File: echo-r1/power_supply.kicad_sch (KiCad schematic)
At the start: 26 parts, among them J1 GT-BTP30003-xxxA-16A, Q2 AO3401A, U1 LM66100DCK, U2 TPS62A01DRLR, U3 TPS62A01DRLR, U4 XC6206P33xMR, U5 TP4057

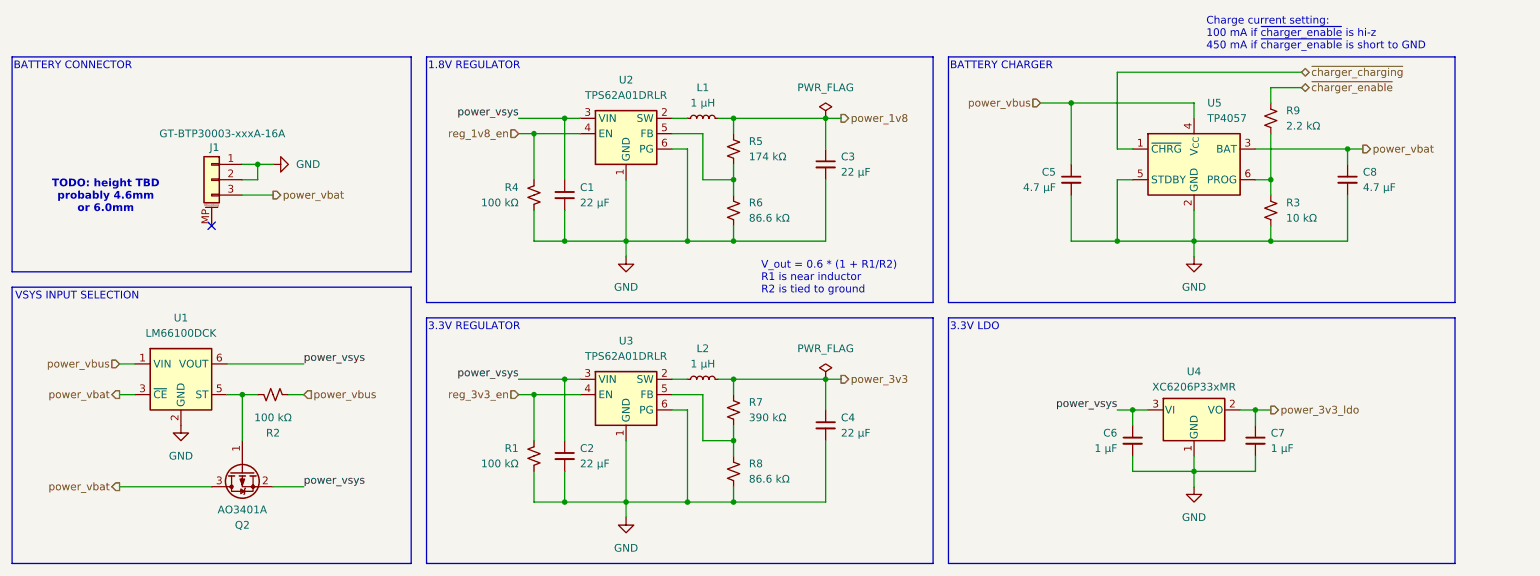
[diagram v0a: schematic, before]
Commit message: WIP redesign with STM32H7R3Z8J6
The H7R3 has a bunch of features that greatly simplify the design:
support for HyperRAM, which requires far fewer pins than SDRAM and
is more power efficient; this frees up the FMC to interface with the
display in 8-bit 8080 MCU mode; and there is a built-in USB HS PHY,
removing the need for an external PHY.

The huge reduction in signal count allows for a smaller pin count
package -- only 144 pins. HyperRAM only comes in BGA packages so it
makes sense to also use the UFBGA-144 package for the CPU, which
takes up less than 1/4 of the board area of an LQFP-176 package.
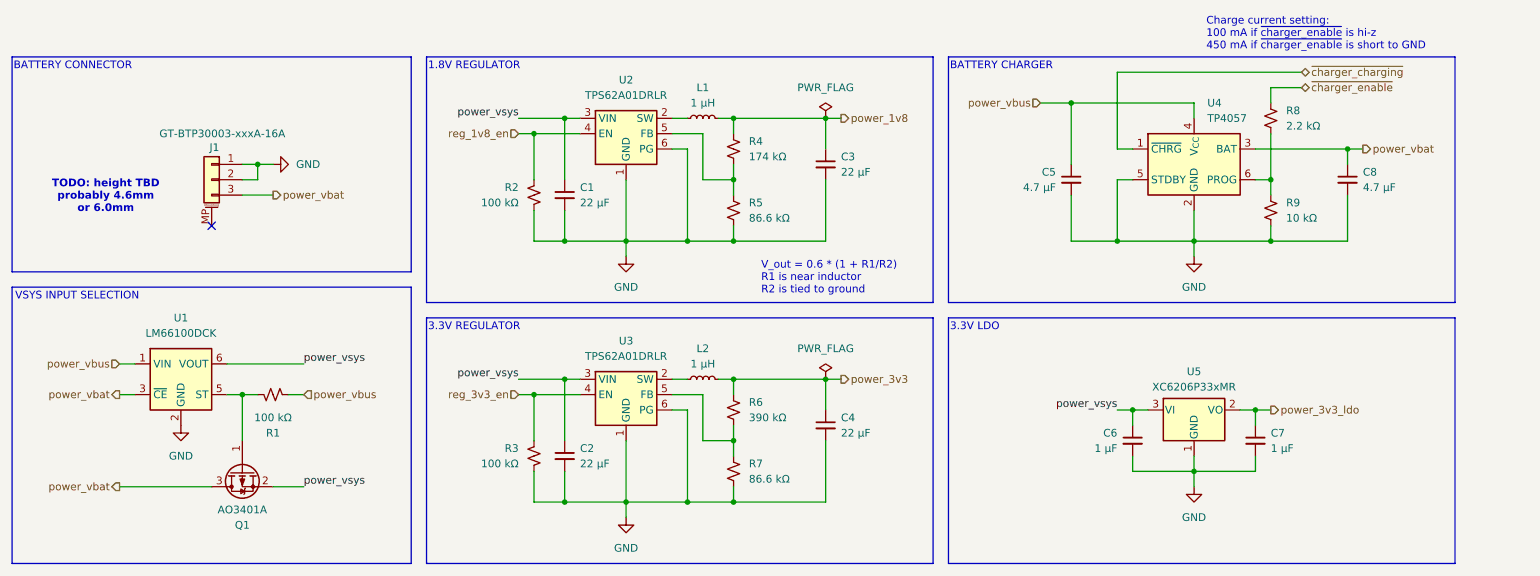
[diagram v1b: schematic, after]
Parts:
- renumbered Q2 to Q1, R2 to R1, R4 to R2, R1 to R3, R5 to R4, R6 to R5, R7 to R6, R8 to R7, R9 to R8, R3 to R9, U5 to U4, U4 to U5
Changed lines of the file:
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@@
 		(dnp no)
 		(fields_autoplaced yes)
-		(property "Reference" "#FLG02"
+		(property "Reference" "#FLG03"
 			(at 162.56 92.075 0)
 			(effects
@@
 			(project "echo-r1"
 				(path "/aa241847-30f4-429d-a148-6a6e39ba98e0/48d39f5c-11a4-46cd-927a-56a9c6ae42fa"
-					(reference "#FLG02")
+					(reference "#FLG03")
 					(unit 1)
 				)
@@
 		(on_board yes)
 		(dnp no)
-		(property "Reference" "R4"
+		(property "Reference" "R2"
 			(at 111.76 62.2299 0)
 			(effects
@@
 			(project "echo-r1"
 				(path "/aa241847-30f4-429d-a148-6a6e39ba98e0/48d39f5c-11a4-46cd-927a-56a9c6ae42fa"
-					(reference "R4")
+					(reference "R2")
 					(unit 1)
 				)
@@
 		(dnp no)
 		(fields_autoplaced yes)
-		(property "Reference" "U5"
+		(property "Reference" "U4"
 			(at 225.7141 48.26 0)
 			(effects
@@
 			(project ""
 				(path "/aa241847-30f4-429d-a148-6a6e39ba98e0/48d39f5c-11a4-46cd-927a-56a9c6ae42fa"
-					(reference "U5")
+					(reference "U4")
 					(unit 1)
 				)
@@
 		(on_board yes)
 		(dnp no)
-		(property "Reference" "R3"
+		(property "Reference" "R9"
 			(at 238.76 64.7699 0)
 			(effects
@@
 			(project "echo-r1"
 				(path "/aa241847-30f4-429d-a148-6a6e39ba98e0/48d39f5c-11a4-46cd-927a-56a9c6ae42fa"
-					(reference "R3")
+					(reference "R9")
 					(unit 1)
 				)
@@
 		(dnp no)
 		(fields_autoplaced yes)
-		(property "Reference" "R6"
+		(property "Reference" "R5"
 			(at 149.86 64.7699 0)
 			(effects
@@
 			(project "echo-r1"
 				(path "/aa241847-30f4-429d-a148-6a6e39ba98e0/48d39f5c-11a4-46cd-927a-56a9c6ae42fa"
-					(reference "R6")
+					(reference "R5")
 					(unit 1)
 				)
@@
 		(on_board yes)
 		(dnp no)
-		(property "Reference" "Q2"
+		(property "Reference" "Q1"
 			(at 66.04 118.11 90)
 			(effects
@@
 			(project "echo-r1"
 				(path "/aa241847-30f4-429d-a148-6a6e39ba98e0/48d39f5c-11a4-46cd-927a-56a9c6ae42fa"
-					(reference "Q2")
+					(reference "Q1")
 					(unit 1)
 				)
@@
 		(dnp no)
 		(fields_autoplaced yes)
-		(property "Reference" "#PWR016"
+		(property "Reference" "#PWR014"
 			(at 223.52 80.01 0)
 			(effects
@@
 			(project ""
 				(path "/aa241847-30f4-429d-a148-6a6e39ba98e0/48d39f5c-11a4-46cd-927a-56a9c6ae42fa"
-					(reference "#PWR016")
+					(reference "#PWR014")
 					(unit 1)
 				)
@@
 		(on_board yes)
 		(dnp no)
-		(property "Reference" "R1"
+		(property "Reference" "R3"
 			(at 111.76 105.4099 0)
 			(effects
@@
 			(project "echo-r1"
 				(path "/aa241847-30f4-429d-a148-6a6e39ba98e0/48d39f5c-11a4-46cd-927a-56a9c6ae42fa"
-					(reference "R1")
+					(reference "R3")
 					(unit 1)
 				)
@@
 		(dnp no)
 		(fields_autoplaced yes)
-		(property "Reference" "R8"
+		(property "Reference" "R7"
 			(at 149.86 107.9499 0)
 			(effects
@@
 			(project "echo-r1"
 				(path "/aa241847-30f4-429d-a148-6a6e39ba98e0/48d39f5c-11a4-46cd-927a-56a9c6ae42fa"
-					(reference "R8")
+					(reference "R7")
 					(unit 1)
 				)
@@
 		(dnp no)
 		(fields_autoplaced yes)
-		(property "Reference" "R7"
+		(property "Reference" "R6"
 			(at 149.86 97.7899 0)
 			(effects
@@
 			(project ""
 				(path "/aa241847-30f4-429d-a148-6a6e39ba98e0/48d39f5c-11a4-46cd-927a-56a9c6ae42fa"
-					(reference "R7")
+					(reference "R6")
 					(unit 1)
 				)
@@
 		(on_board yes)
 		(dnp no)
-		(property "Reference" "R9"
+		(property "Reference" "R8"
 			(at 238.76 49.5299 0)
 			(effects
@@
 			(project "echo-r1"
 				(path "/aa241847-30f4-429d-a148-6a6e39ba98e0/48d39f5c-11a4-46cd-927a-56a9c6ae42fa"
-					(reference "R9")
+					(reference "R8")
 					(unit 1)
 				)
@@
 		(dnp no)
 		(fields_autoplaced yes)
-		(property "Reference" "#PWR013"
+		(property "Reference" "#PWR012"
 			(at 129.54 80.01 0)
 			(effects
@@
 			(project "echo-r1"
 				(path "/aa241847-30f4-429d-a148-6a6e39ba98e0/48d39f5c-11a4-46cd-927a-56a9c6ae42fa"
-					(reference "#PWR013")
+					(reference "#PWR012")
 					(unit 1)
 				)
@@
 		(dnp no)
 		(fields_autoplaced yes)
-		(property "Reference" "R5"
+		(property "Reference" "R4"
 			(at 149.86 54.6099 0)
 			(effects
@@
 			(project "echo-r1"
 				(path "/aa241847-30f4-429d-a148-6a6e39ba98e0/48d39f5c-11a4-46cd-927a-56a9c6ae42fa"
-					(reference "R5")
+					(reference "R4")
 					(unit 1)
 				)
@@
 		(dnp no)
 		(fields_autoplaced yes)
-		(property "Reference" "#PWR014"
+		(property "Reference" "#PWR013"
 			(at 129.54 123.19 0)
 			(effects
@@
 			(project ""
 				(path "/aa241847-30f4-429d-a148-6a6e39ba98e0/48d39f5c-11a4-46cd-927a-56a9c6ae42fa"
-					(reference "#PWR014")
+					(reference "#PWR013")
 					(unit 1)
 				)
@@
 		(on_board yes)
 		(dnp no)
-		(property "Reference" "R2"
+		(property "Reference" "R1"
 			(at 71.12 102.87 90)
 			(effects
@@
 			(project "echo-r1"
 				(path "/aa241847-30f4-429d-a148-6a6e39ba98e0/48d39f5c-11a4-46cd-927a-56a9c6ae42fa"
-					(reference "R2")
+					(reference "R1")
 					(unit 1)
 				)
@@
 		(dnp no)
 		(fields_autoplaced yes)
-		(property "Reference" "#FLG01"
+		(property "Reference" "#FLG02"
 			(at 162.56 48.895 0)
 			(effects
@@
 			(project ""
 				(path "/aa241847-30f4-429d-a148-6a6e39ba98e0/48d39f5c-11a4-46cd-927a-56a9c6ae42fa"
-					(reference "#FLG01")
+					(reference "#FLG02")
 					(unit 1)
 				)
@@
 		(dnp no)
 		(fields_autoplaced yes)
-		(property "Reference" "U4"
+		(property "Reference" "U5"
 			(at 223.52 92.71 0)
 			(effects
@@
 			(project ""
 				(path "/aa241847-30f4-429d-a148-6a6e39ba98e0/48d39f5c-11a4-46cd-927a-56a9c6ae42fa"
-					(reference "U4")
-					(unit 1)
-				)
+					(reference "U5")
+					(unit 1)
+				)

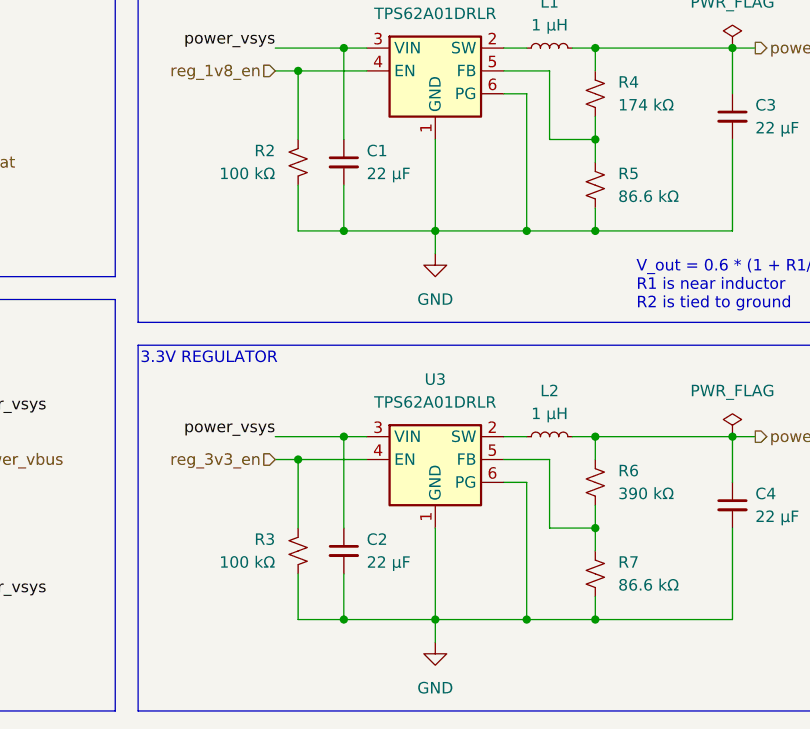
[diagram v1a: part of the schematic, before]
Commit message: Continue with redesign, update and simplify schematic
- Consolidate small sheets (ports, etc) onto one page
- Add placeholders for STM32 external components
- Add power switch on SD card for resetting it
- Fix oversized input capacitors on voltage regulators
- Get rid of unique 1M resistor used in line-out detection
- Remove SOT23 TVS diodes (will be replaced by another package)
- Update LCD connector symbol for new 30pin screen
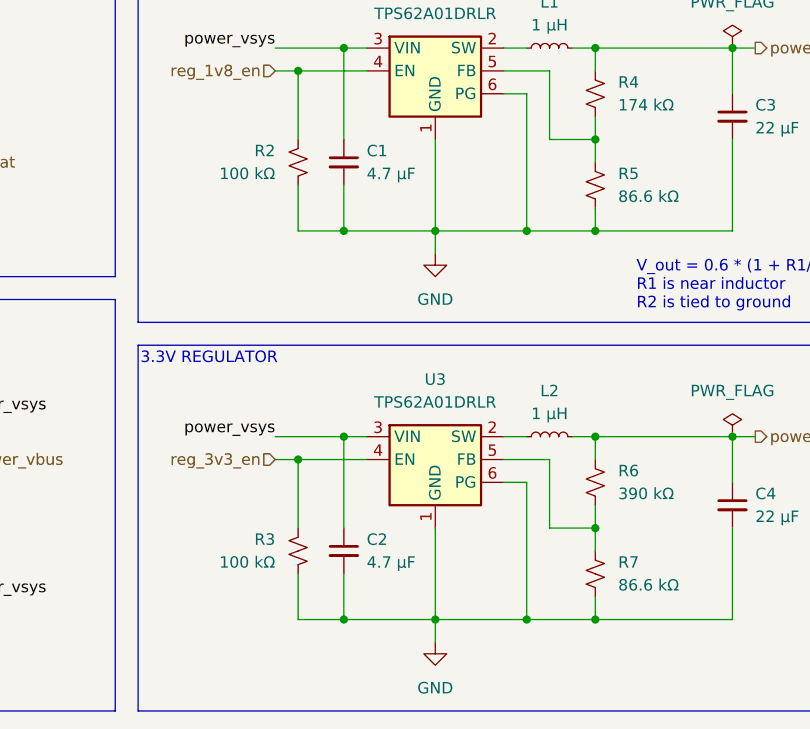
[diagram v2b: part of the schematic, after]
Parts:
- C1, C2: value 22 µF -> 4.7 µF
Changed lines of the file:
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@@
 		(title "Power supply / battery charger")
 		(date "2024-11-14")
-		(rev "Rev1")
+		(rev "Rev2")
 		(comment 1 "Author: Aidan MacDonald")
 	)
@@
 			)
 		)
-		(property "Value" "22 µF"
+		(property "Value" "4.7 µF"
 			(at 121.92 107.9562 0)
 			(effects
@@
 			)
 		)
-		(property "Value" "22 µF"
+		(property "Value" "4.7 µF"
 			(at 121.92 64.7762 0)
 			(effects
